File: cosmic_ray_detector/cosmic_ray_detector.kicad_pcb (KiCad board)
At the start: 4 copper layers, 66.5 x 45 mm, 51 parts, among them J1 MOLEX micro-fit 43045-0210, J2 5 pin pin header, J3 Black Banana, J4 Red Banana, J5 Green Banana, J6 BNC, U1 TL072, U2 TPS7A30, U3 TPS7A49, U4 TLV3501AIDBVTG4, U5 AD5270BRMZ-100-RL7

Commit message: pcb placement underway
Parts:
- moved C11 128.7 mm to (96.8, 97.2)
- moved C12 119.3 mm to (103.5, 110.5)
- moved R7 119.2 mm to (91.0, 108.5)
- moved C14 105.1 mm to (100.0, 117.6)
- moved R11 88.8 mm to (149.7, 55.8), turned to 180 degrees
- moved R9 69.3 mm to (147.6, 55.3), turned to 90 degrees
- moved C8 68.9 mm to (138.0, 52.8), turned to 180 degrees
- moved C16 66.3 mm to (156.2, 101.8)
- moved R6 65.4 mm to (157.1, 97.9)
- moved C13 65.4 mm to (160.0, 98.2)
- moved R4 63.3 mm to (138.0, 54.0), turned to 180 degrees
- moved C17 60.2 mm to (143.0, 44.4)
- moved C18 60.2 mm to (140.1, 46.4)
- moved R5 57.6 mm to (154.8, 98.0)
- moved R3 56.7 mm to (140.0, 65.0)
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
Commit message: blank PCB, ready to populate
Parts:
- removed C1: C, Capacitor_SMD:C_1210_3225Metric
- removed C10, C15, C2, C21, C3, C9: 10uF, cosmic_ray_detector_lib:MAL215375109E3
- removed C11, C12: 22nF, Capacitor_SMD:C_0402_1005Metric
- removed C13, C14, C16: 10nF, Capacitor_SMD:C_0402_1005Metric
- removed C17, C20, C4, C5: 0.1uF, Capacitor_SMD:C_0402_1005Metric
- removed C18: 2.2uF, Capacitor_SMD:C_0402_1005Metric
- removed C19: 1uF, Capacitor_SMD:C_0402_1005Metric
- removed C6: C, Capacitor_SMD:C_0402_1005Metric
- removed C7, C8: ~, Capacitor_SMD:C_0402_1005Metric
- removed D1: VBPW34FAS, cosmic_ray_detector_lib:VBPW34FAS
- removed D2, D3: 12V, Diode_SMD:D_SOD-123
- removed J1: MOLEX micro-fit 43045-0210, cosmic_ray_detector_lib:4304502_09
- removed J2: 5 pin pin header, Connector_PinHeader_1.27mm:PinHeader_1x05_P1.27mm_Vertical
- removed J3: Black Banana, cosmic_ray_detector_lib:242432
- removed J4: Red Banana, cosmic_ray_detector_lib:242431
- removed J5: Green Banana, cosmic_ray_detector_lib:242434
- removed J6: BNC, cosmic_ray_detector_lib:MOLEX_731375003
- removed L1, L2: L, Inductor_SMD:L_1008_2520Metric
- removed R1, R10, R11, R2: R_US, Resistor_SMD:R_0402_1005Metric
- removed R3, R4, R9: ~, Resistor_SMD:R_0402_1005Metric
- removed R5: 13k, Resistor_SMD:R_0402_1005Metric
- removed R6, R8: 10k, Resistor_SMD:R_0402_1005Metric
- removed R7: 12.7k, Resistor_SMD:R_0402_1005Metric
- removed TP1: TestPoint, cosmic_ray_detector_lib:harwin_tp_SMD
- removed TP2, TP3: ~, cosmic_ray_detector_lib:harwin_tp_SMD
- removed U1: TL072, Package_SO:SO-8_3.9x4.9mm_P1.27mm
- removed U2: TPS7A30, cosmic_ray_detector_lib:MSOP-8-1EP_3x3mm_P0.65mm_EP1.73x1.85mm_ThermalVias
- removed U3: TPS7A49, cosmic_ray_detector_lib:MSOP-8-1EP_3x3mm_P0.65mm_EP1.73x1.85mm_ThermalVias
- removed U4: TLV3501AIDBVTG4, cosmic_ray_detector_lib:SOT95P280X145-6N
- removed U5: AD5270BRMZ-100-RL7, cosmic_ray_detector_lib:SOP50P490X110-10N
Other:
- board outline removed

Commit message: components imported, outline drawn
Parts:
- added C1: C, Capacitor_SMD:C_1210_3225Metric, F.Cu at (187.1, 63.9)
- added C10: 10uF, cosmic_ray_detector_lib:MAL215375109E3, F.Cu at (235.0, 135.0)
- added C11: 22nF, Capacitor_SMD:C_0402_1005Metric, F.Cu at (238.2, 149.6)
- added C12: 22nF, Capacitor_SMD:C_0402_1005Metric, F.Cu at (232.5, 154.9)
- added C13: 10nF, Capacitor_SMD:C_0402_1005Metric, F.Cu at (251.3, 136.3)
- added C14: 10nF, Capacitor_SMD:C_0402_1005Metric, F.Cu at (239.7, 147.0)
- added C15: 10uF, cosmic_ray_detector_lib:MAL215375109E3, F.Cu at (235.0, 141.1)
- added C16: 10nF, Capacitor_SMD:C_0402_1005Metric, F.Cu at (254.1, 133.0)
- added C17: 0.1uF, Capacitor_SMD:C_0402_1005Metric, F.Cu at (235.4, 97.1)
- added C18: 2.2uF, Capacitor_SMD:C_0402_1005Metric, F.Cu at (232.5, 99.1)
- added C19: 1uF, Capacitor_SMD:C_0402_1005Metric, F.Cu at (203.4, 103.2)
- added C2: 10uF, cosmic_ray_detector_lib:MAL215375109E3, F.Cu at (205.9, 148.4)
- added C20: 0.1uF, Capacitor_SMD:C_0402_1005Metric, F.Cu at (211.3, 94.5)
- added C21: 10uF, cosmic_ray_detector_lib:MAL215375109E3, F.Cu at (205.9, 94.6)
- added C3: 10uF, cosmic_ray_detector_lib:MAL215375109E3, F.Cu at (218.9, 135.0)
- added C4: 0.1uF, Capacitor_SMD:C_0402_1005Metric, F.Cu at (224.4, 134.9)
- added C5: 0.1uF, Capacitor_SMD:C_0402_1005Metric, F.Cu at (220.9, 141.0)
- added C6: C, Capacitor_SMD:C_0402_1005Metric, F.Cu at (224.4, 136.9)
- added C7: ~, Capacitor_SMD:C_0402_1005Metric, F.Cu at (218.0, 141.0)
- added C8: ~, Capacitor_SMD:C_0402_1005Metric, F.Cu at (218.0, 143.0)
- added C9: 10uF, cosmic_ray_detector_lib:MAL215375109E3, F.Cu at (243.0, 135.0)
- added D1: VBPW34FAS, cosmic_ray_detector_lib:VBPW34FAS, F.Cu at (209.0, 135.5)
- added D2: 12V, Diode_SMD:D_SOD-123, F.Cu at (233.9, 150.3)
- added D3: 12V, Diode_SMD:D_SOD-123, F.Cu at (249.8, 133.6)
- added J1: MOLEX micro-fit 43045-0210, cosmic_ray_detector_lib:4304502_09, F.Cu at (207.5, 57.1)
- added J2: 5 pin pin header, Connector_PinHeader_1.27mm:PinHeader_1x05_P1.27mm_Vertical, F.Cu at (231.3, 38.3)
- added J3: Black Banana, cosmic_ray_detector_lib:242432, F.Cu at (235.0, 30.0)
- added J4: Red Banana, cosmic_ray_detector_lib:242431, F.Cu at (207.9, 30.0)
- added J5: Green Banana, cosmic_ray_detector_lib:242434, F.Cu at (207.9, 43.3)
- added J6: BNC, cosmic_ray_detector_lib:MOLEX_731375003, F.Cu at (193.2, 25.7)
- added L1: L, Inductor_SMD:L_1008_2520Metric, F.Cu at (192.4, 63.7)
- added L2: L, Inductor_SMD:L_1008_2520Metric, F.Cu at (197.3, 63.7)
- added NT1: NetTie_2, NetTie:NetTie-2_SMD_Pad0.5mm, F.Cu at (191.4, 66.6)
- added R1: R_US, Resistor_SMD:R_0402_1005Metric, F.Cu at (194.4, 66.5)
- added R10: R_US, Resistor_SMD:R_0402_1005Metric, F.Cu at (237.7, 92.6)
- added R11: R_US, Resistor_SMD:R_0402_1005Metric, F.Cu at (211.3, 92.6)
- added R2: R_US, Resistor_SMD:R_0402_1005Metric, F.Cu at (218.0, 139.0)
- added R3: ~, Resistor_SMD:R_0402_1005Metric, F.Cu at (211.3, 147.9)
- added R4: ~, Resistor_SMD:R_0402_1005Metric, F.Cu at (224.4, 133.0)
- added R5: 13k, Resistor_SMD:R_0402_1005Metric, F.Cu at (247.7, 139.0)
- added R6: 10k, Resistor_SMD:R_0402_1005Metric, F.Cu at (232.5, 153.0)
- added R7: 12.7k, Resistor_SMD:R_0402_1005Metric, F.Cu at (248.4, 136.3)
- added R8: 10k, Resistor_SMD:R_0402_1005Metric, F.Cu at (239.8, 145.1)
- added R9: ~, Resistor_SMD:R_0402_1005Metric, F.Cu at (232.5, 97.2)
- added TP1: TestPoint, cosmic_ray_detector_lib:harwin_tp_SMD, F.Cu at (213.1, 140.9)
- added TP2: ~, cosmic_ray_detector_lib:harwin_tp_SMD, F.Cu at (213.1, 144.9)
- added TP3: ~, cosmic_ray_detector_lib:harwin_tp_SMD, F.Cu at (204.7, 153.4)
- added U1: TL072, Package_SO:SO-8_3.9x4.9mm_P1.27mm, F.Cu at (206.1, 142.2)
- added U2: TPS7A30, cosmic_ray_detector_lib:MSOP-8-1EP_3x3mm_P0.65mm_EP1.73x1.85mm_ThermalVias, F.Cu at (234.7, 146.3)
- added U3: TPS7A49, cosmic_ray_detector_lib:MSOP-8-1EP_3x3mm_P0.65mm_EP1.73x1.85mm_ThermalVias, F.Cu at (242.6, 140.3)
- added U4: TLV3501AIDBVTG4, cosmic_ray_detector_lib:SOT95P280X145-6N, F.Cu at (233.6, 93.9)
- added U5: AD5270BRMZ-100-RL7, cosmic_ray_detector_lib:SOP50P490X110-10N, F.Cu at (205.6, 99.9)
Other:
- board outline added: 80 x 60 mm

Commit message: setup design rules & netclasses for Newbury
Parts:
- removed C1: C, Capacitor_SMD:C_1210_3225Metric
- removed C10, C15, C2, C21, C3, C9: 10uF, cosmic_ray_detector_lib:MAL215375109E3
- removed C11, C12: 22nF, Capacitor_SMD:C_0402_1005Metric
- removed C13, C14, C16: 10nF, Capacitor_SMD:C_0402_1005Metric
- removed C17, C20, C4, C5: 0.1uF, Capacitor_SMD:C_0402_1005Metric
- removed C18: 2.2uF, Capacitor_SMD:C_0402_1005Metric
- removed C19: 1uF, Capacitor_SMD:C_0402_1005Metric
- removed C6: C, Capacitor_SMD:C_0402_1005Metric
- removed C7, C8: ~, Capacitor_SMD:C_0402_1005Metric
- removed D1: VBPW34FAS, cosmic_ray_detector_lib:VBPW34FAS
- removed D2, D3: 12V, Diode_SMD:D_SOD-123
- removed J1: MOLEX micro-fit 43045-0210, cosmic_ray_detector_lib:4304502_09
- removed J2: 5 pin pin header, Connector_PinHeader_1.27mm:PinHeader_1x05_P1.27mm_Vertical
- removed J3: Black Banana, cosmic_ray_detector_lib:242432
- removed J4: Red Banana, cosmic_ray_detector_lib:242431
- removed J5: Green Banana, cosmic_ray_detector_lib:242434
- removed J6: BNC, cosmic_ray_detector_lib:MOLEX_731375003
- removed L1, L2: L, Inductor_SMD:L_1008_2520Metric
- removed NT1: NetTie_2, NetTie:NetTie-2_SMD_Pad0.5mm
- removed R1, R10, R11, R2: R_US, Resistor_SMD:R_0402_1005Metric
- removed R3, R4, R9: ~, Resistor_SMD:R_0402_1005Metric
- removed R5: 13k, Resistor_SMD:R_0402_1005Metric
- removed R6, R8: 10k, Resistor_SMD:R_0402_1005Metric
- removed R7: 12.7k, Resistor_SMD:R_0402_1005Metric
- removed TP1: TestPoint, cosmic_ray_detector_lib:harwin_tp_SMD
- removed TP2, TP3: ~, cosmic_ray_detector_lib:harwin_tp_SMD
- removed U1: TL072, Package_SO:SO-8_3.9x4.9mm_P1.27mm
- removed U2: TPS7A30, cosmic_ray_detector_lib:MSOP-8-1EP_3x3mm_P0.65mm_EP1.73x1.85mm_ThermalVias
- removed U3: TPS7A49, cosmic_ray_detector_lib:MSOP-8-1EP_3x3mm_P0.65mm_EP1.73x1.85mm_ThermalVias
- removed U4: TLV3501AIDBVTG4, cosmic_ray_detector_lib:SOT95P280X145-6N
- removed U5: AD5270BRMZ-100-RL7, cosmic_ray_detector_lib:SOP50P490X110-10N
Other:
- board outline removed

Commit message: import from schem and draw outline and some mounting holes
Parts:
- added C1: C, Capacitor_SMD:C_1210_3225Metric, F.Cu at (180.5, 63.5)
- added C10: 10uF, cosmic_ray_detector_lib:MAL215375109E3, F.Cu at (228.4, 134.5)
- added C11: 22nF, Capacitor_SMD:C_0402_1005Metric, F.Cu at (231.6, 149.2)
- added C12: 22nF, Capacitor_SMD:C_0402_1005Metric, F.Cu at (225.8, 154.5)
- added C13: 10nF, Capacitor_SMD:C_0402_1005Metric, F.Cu at (244.7, 135.8)
- added C14: 10nF, Capacitor_SMD:C_0402_1005Metric, F.Cu at (233.1, 146.6)
- added C15: 10uF, cosmic_ray_detector_lib:MAL215375109E3, F.Cu at (228.4, 140.6)
- added C16: 10nF, Capacitor_SMD:C_0402_1005Metric, F.Cu at (247.5, 132.5)
- added C17: 0.1uF, Capacitor_SMD:C_0402_1005Metric, F.Cu at (228.7, 96.7)
- added C18: 2.2uF, Capacitor_SMD:C_0402_1005Metric, F.Cu at (225.8, 98.7)
- added C19: 1uF, Capacitor_SMD:C_0402_1005Metric, F.Cu at (196.7, 102.8)
- added C2: 10uF, cosmic_ray_detector_lib:MAL215375109E3, F.Cu at (199.3, 148.0)
- added C20: 0.1uF, Capacitor_SMD:C_0402_1005Metric, F.Cu at (204.7, 94.1)
- added C21: 10uF, cosmic_ray_detector_lib:MAL215375109E3, F.Cu at (199.3, 94.1)
- added C3: 10uF, cosmic_ray_detector_lib:MAL215375109E3, F.Cu at (212.3, 134.5)
- added C4: 0.1uF, Capacitor_SMD:C_0402_1005Metric, F.Cu at (217.7, 134.5)
- added C5: 0.1uF, Capacitor_SMD:C_0402_1005Metric, F.Cu at (214.3, 140.5)
- added C6: C, Capacitor_SMD:C_0402_1005Metric, F.Cu at (217.7, 136.5)
- added C7: ~, Capacitor_SMD:C_0402_1005Metric, F.Cu at (211.4, 140.5)
- added C8: ~, Capacitor_SMD:C_0402_1005Metric, F.Cu at (211.4, 142.5)
- added C9: 10uF, cosmic_ray_detector_lib:MAL215375109E3, F.Cu at (236.3, 134.5)
- added D1: VBPW34FAS, cosmic_ray_detector_lib:VBPW34FAS, F.Cu at (202.3, 135.0)
- added D2: 12V, Diode_SMD:D_SOD-123, F.Cu at (227.3, 149.8)
- added D3: 12V, Diode_SMD:D_SOD-123, F.Cu at (243.2, 133.2)
- added J1: MOLEX micro-fit 43045-0210, cosmic_ray_detector_lib:4304502_09, F.Cu at (200.9, 56.6)
- added J2: 5 pin pin header, Connector_PinHeader_1.27mm:PinHeader_1x05_P1.27mm_Vertical, F.Cu at (224.7, 37.9)
- added J3: Black Banana, cosmic_ray_detector_lib:242432, F.Cu at (228.4, 29.5)
- added J4: Red Banana, cosmic_ray_detector_lib:242431, F.Cu at (201.3, 29.5)
- added J5: Green Banana, cosmic_ray_detector_lib:242434, F.Cu at (201.3, 42.8)
- added J6: BNC, cosmic_ray_detector_lib:MOLEX_731375003, F.Cu at (126.0, 82.0)
- added L1: L, Inductor_SMD:L_1008_2520Metric, F.Cu at (185.8, 63.2)
- added L2: L, Inductor_SMD:L_1008_2520Metric, F.Cu at (190.7, 63.2)
- added NT1: NetTie_2, NetTie:NetTie-2_SMD_Pad0.5mm, F.Cu at (184.8, 66.1)
- added R1: R_US, Resistor_SMD:R_0402_1005Metric, F.Cu at (187.8, 66.1)
- added R10: R_US, Resistor_SMD:R_0402_1005Metric, F.Cu at (231.1, 92.1)
- added R11: R_US, Resistor_SMD:R_0402_1005Metric, F.Cu at (204.7, 92.1)
- added R2: R_US, Resistor_SMD:R_0402_1005Metric, F.Cu at (211.4, 138.6)
- added R3: ~, Resistor_SMD:R_0402_1005Metric, F.Cu at (204.7, 147.4)
- added R4: ~, Resistor_SMD:R_0402_1005Metric, F.Cu at (217.8, 132.5)
- added R5: 13k, Resistor_SMD:R_0402_1005Metric, F.Cu at (241.1, 138.6)
- added R6: 10k, Resistor_SMD:R_0402_1005Metric, F.Cu at (225.8, 152.5)
- added R7: 12.7k, Resistor_SMD:R_0402_1005Metric, F.Cu at (241.8, 135.9)
- added R8: 10k, Resistor_SMD:R_0402_1005Metric, F.Cu at (233.1, 144.6)
- added R9: ~, Resistor_SMD:R_0402_1005Metric, F.Cu at (225.8, 96.7)
- added REF**: MountingHole_3.2mm_M3_ISO14580, MountingHole:MountingHole_3.2mm_M3_ISO14580, F.Cu at (63.4, 59.5)
- added REF**: MountingHole_3.2mm_M3_ISO14580, MountingHole:MountingHole_3.2mm_M3_ISO14580, F.Cu at (133.4, 59.5)
- added REF**: MountingHole_3.2mm_M3_ISO14580, MountingHole:MountingHole_3.2mm_M3_ISO14580, F.Cu at (63.4, 109.5)
- added REF**: MountingHole_3.2mm_M3_ISO14580, MountingHole:MountingHole_3.2mm_M3_ISO14580, F.Cu at (133.4, 109.5)
- added TP1: TestPoint, cosmic_ray_detector_lib:harwin_tp_SMD, F.Cu at (206.5, 140.5)
- added TP2: ~, cosmic_ray_detector_lib:harwin_tp_SMD, F.Cu at (206.5, 144.4)
- added TP3: ~, cosmic_ray_detector_lib:harwin_tp_SMD, F.Cu at (198.1, 153.0)
- added U1: TL072, Package_SO:SO-8_3.9x4.9mm_P1.27mm, F.Cu at (199.5, 141.7)
- added U2: TPS7A30, cosmic_ray_detector_lib:MSOP-8-1EP_3x3mm_P0.65mm_EP1.73x1.85mm_ThermalVias, F.Cu at (228.0, 145.9)
- added U3: TPS7A49, cosmic_ray_detector_lib:MSOP-8-1EP_3x3mm_P0.65mm_EP1.73x1.85mm_ThermalVias, F.Cu at (236.0, 139.8)
- added U4: TLV3501AIDBVTG4, cosmic_ray_detector_lib:SOT95P280X145-6N, F.Cu at (227.0, 93.4)
- added U5: AD5270BRMZ-100-RL7, cosmic_ray_detector_lib:SOP50P490X110-10N, F.Cu at (199.0, 99.5)
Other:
- board outline added: 80 x 60 mm

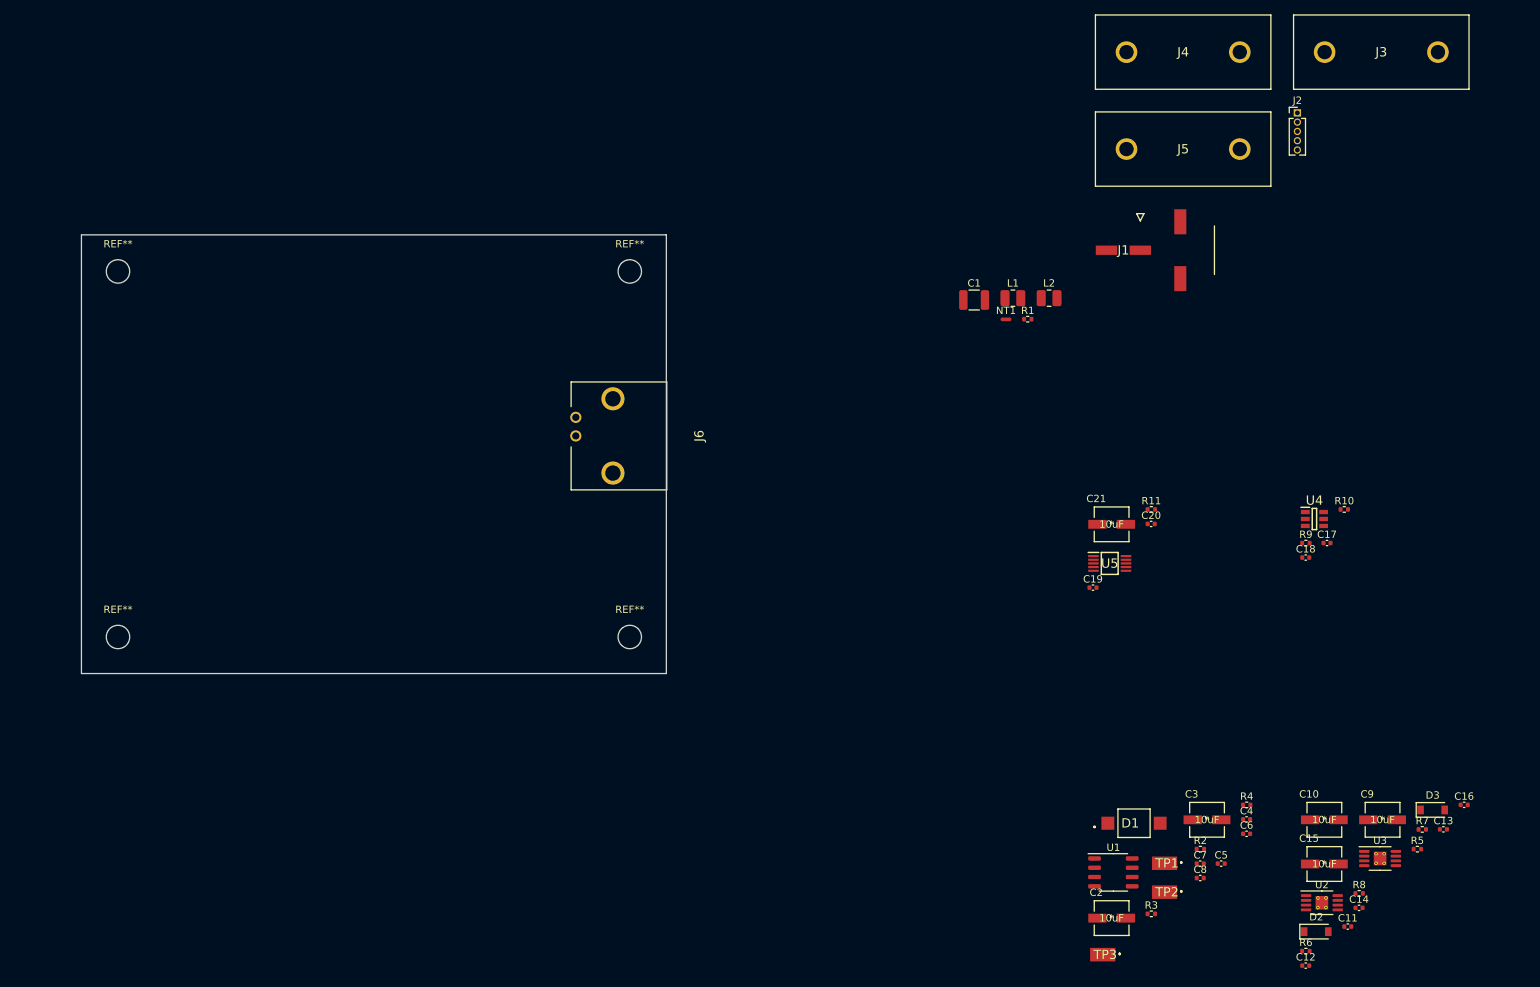
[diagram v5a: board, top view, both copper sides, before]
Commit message: change capacitor footprint, place and add zones for +- LDO regs
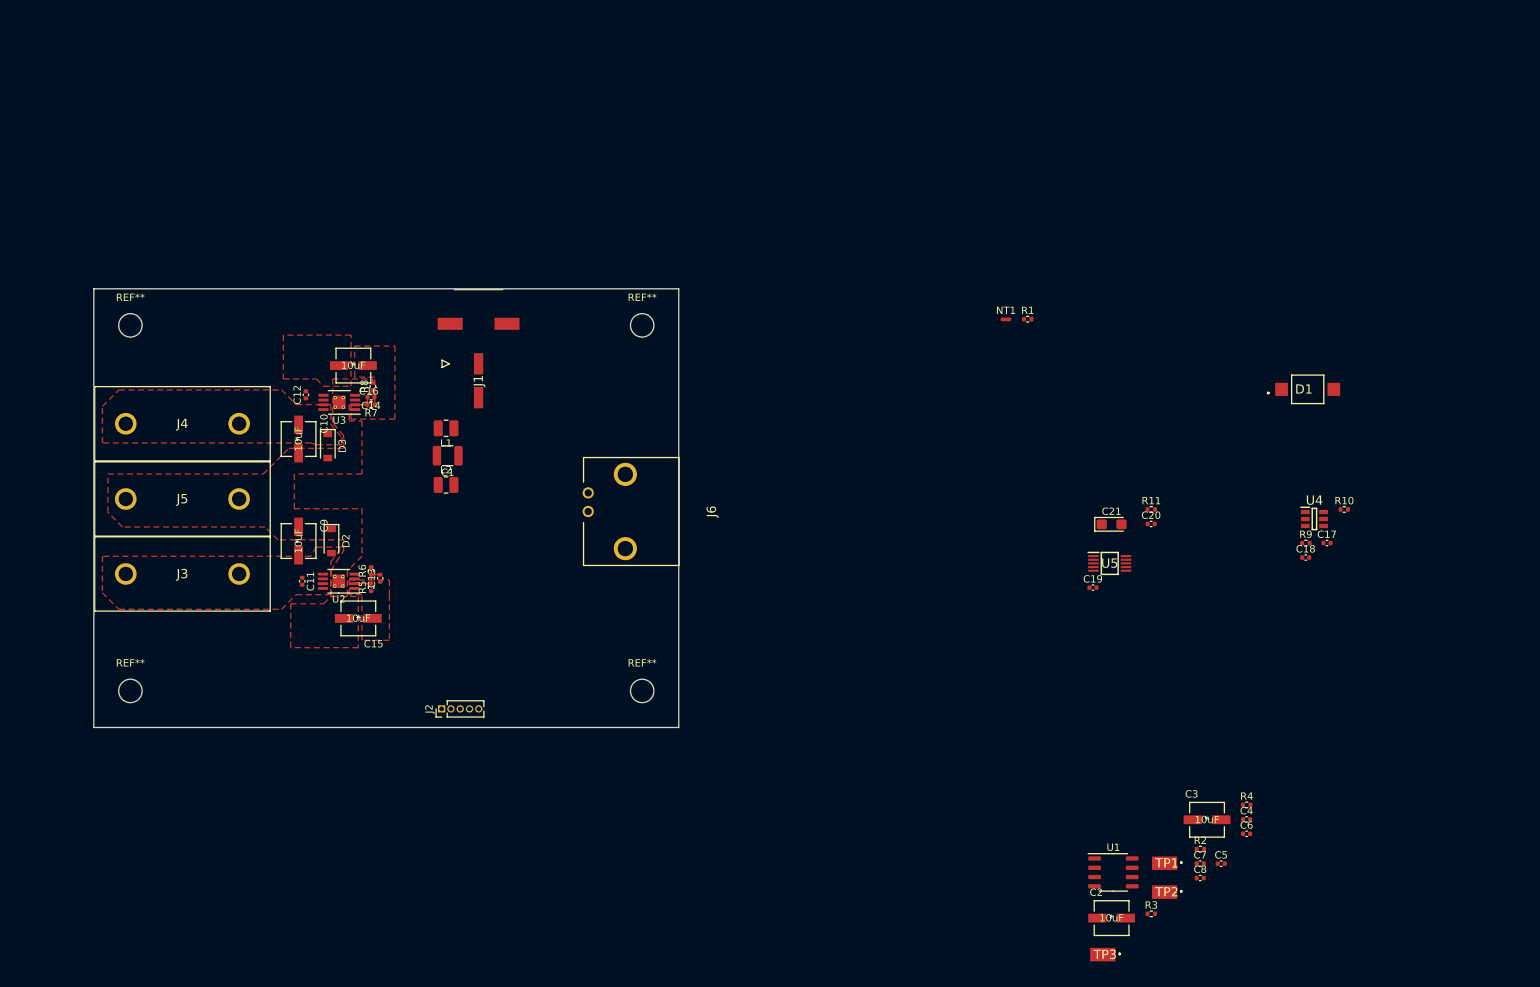
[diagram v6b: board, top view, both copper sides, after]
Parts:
- removed the REF** at (63.4, 59.5)
- removed the REF** at (133.4, 59.5)
- removed the REF** at (63.4, 109.5)
- removed the REF** at (133.4, 109.5)
- added REF**: MountingHole_3.2mm_M3_DIN965, MountingHole:MountingHole_3.2mm_M3_DIN965, F.Cu at (135.1, 66.9)
- added REF**: MountingHole_3.2mm_M3_DIN965, MountingHole:MountingHole_3.2mm_M3_DIN965, F.Cu at (135.1, 116.9)
- added REF**: MountingHole_3.2mm_M3_DIN965, MountingHole:MountingHole_3.2mm_M3_DIN965, F.Cu at (65.1, 66.9)
- added REF**: MountingHole_3.2mm_M3_DIN965, MountingHole:MountingHole_3.2mm_M3_DIN965, F.Cu at (65.1, 116.9)
- C16: value 10nF -> 10uF; footprint Capacitor_SMD:C_0402_1005Metric -> cosmic_ray_detector_lib:MAL215375109E3
- C21: footprint cosmic_ray_detector_lib:MAL215375109E3 -> Capacitor_Tantalum_SMD:CP_EIA-3216-12_Kemet-S
- moved J3 178.8 mm to (64.4, 100.9)
- moved C16 163.4 mm to (95.6, 72.4), turned to 180 degrees
- moved D3 159.1 mm to (92.1, 83.4), turned to -90 degrees
- moved C12 157.5 mm to (89.1, 76.4), turned to 90 degrees
- moved U3 155.4 mm to (93.6, 77.5), turned to 180 degrees
- moved R7 155.1 mm to (98.0, 77.8), turned to 180 degrees
- moved C9 153.1 mm to (88.1, 96.4), turned to -90 degrees
- moved C14 152.1 mm to (98.0, 76.8), turned to 180 degrees
- moved R8 151.7 mm to (98.2, 75.3), turned to 90 degrees
- moved C11 150.6 mm to (88.6, 101.9), turned to -90 degrees
- moved C10 149.7 mm to (88.1, 82.5), turned to -90 degrees
- moved C13 149.4 mm to (99.2, 101.5), turned to 90 degrees
- moved R5 147.5 mm to (98.0, 102.8), turned to 90 degrees
- moved J4 146.0 mm to (64.4, 80.4)
- moved J5 145.0 mm to (64.4, 90.7)
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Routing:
- net Net-(C13-Pad2): track 0.00 -> 4.75 mm
- net Net-(C14-Pad2): track 0.00 -> 3.99 mm
- added copper zone on F.Cu, net +5VA
- added copper zone on F.Cu, net -5VA
- added copper zone on F.Cu, net /Power Regulators/+VIN
- added copper zone on F.Cu, net /Power Regulators/-VIN
- added copper zone on F.Cu, net GNDA
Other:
- board text added: "NOTE: Always follow datasheet recommendations on layout, especially for regulators & the like. Here, note that the pin {dblquote}5{dblquote} is just the {dblquote}enable{dblquote} pin, we really want all the current through VIN net to go to pin 8"
